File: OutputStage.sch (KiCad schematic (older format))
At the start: 83 parts, among them Q12 BSC067N06LS3, Q13 BSC067N06LS3, Q3 AON7400A, Q5 AON7400A, U5 LM5175PWPR

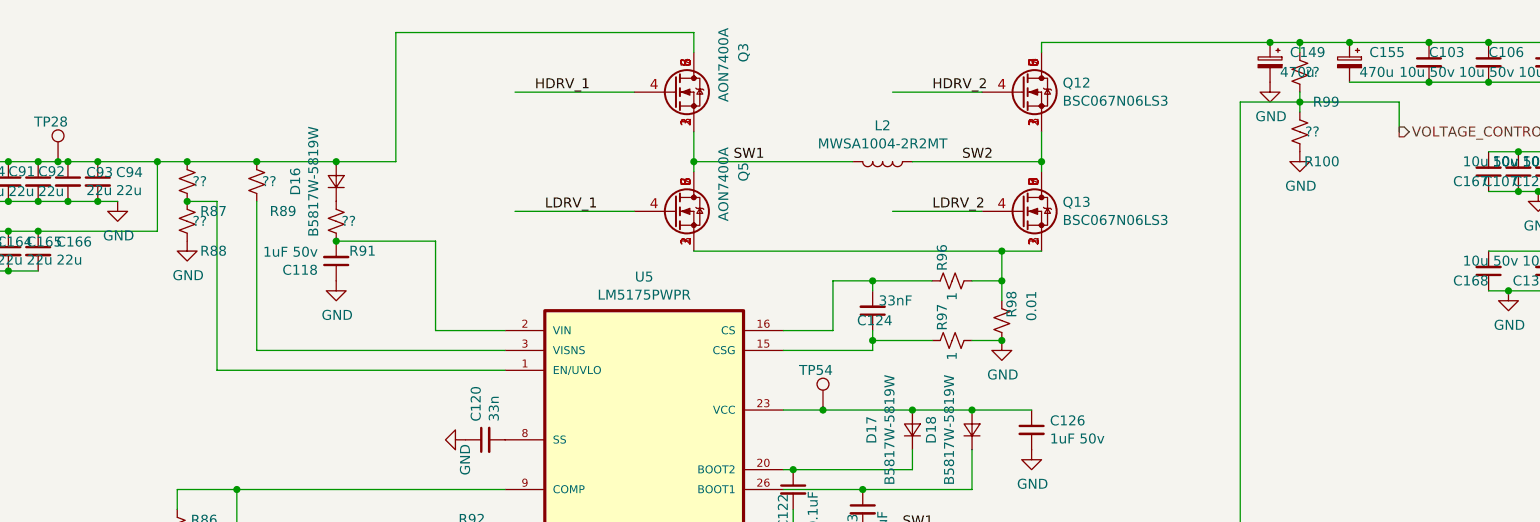
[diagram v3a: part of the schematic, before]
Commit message: Modified connections, added current limit
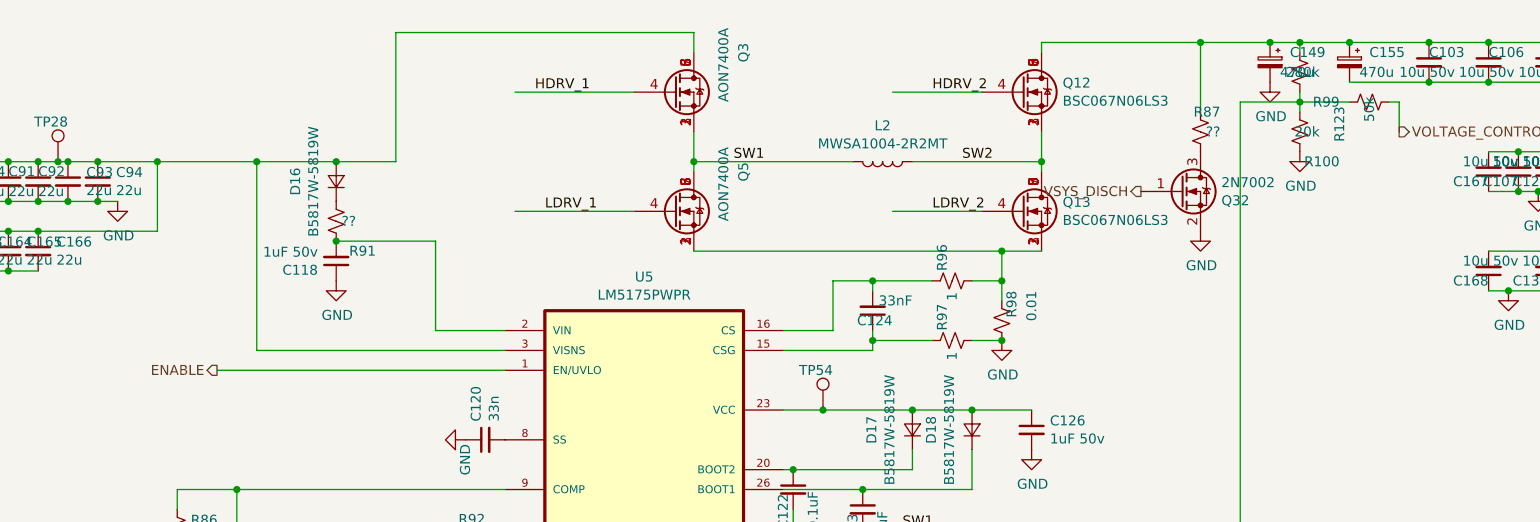
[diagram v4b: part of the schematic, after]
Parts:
- removed R88, R89: ??, lc_lib:0402_R, symbol Device:R_Small_US
- added Q32: 2N7002, Package_TO_SOT_SMD:SOT-23, symbol Device:Q_NMOS_GSD
- added R123: 50k, lc_lib:0402_R, symbol Device:R_Small_US
- R100: value ?? -> 20k
- R99: value ?? -> 280k
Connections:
- net labels added: ENABLE, VSYS_DISCH
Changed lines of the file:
@@
 	2250 1150 2550 1150
 Connection ~ 2250 1150
-$Comp
-L Device:R_Small_US R?
-U 1 1 5FFCD88F
-P 2700 1250
-AR Path="/5FD99B08/5FFCD88F" Ref="R?"  Part="1"
-AR Path="/60413DD6/5FFCD88F" Ref="R87"  Part="1"
-F 0 "R87" H 2500 1400 50  0000 L CNN
-F 1 "??" H 2600 1250 50  0000 L CNN
-F 2 "lc_lib:0402_R" H 2700 1250 50  0001 C CNN
-F 3 "~" H 2700 1250 50  0001 C CNN
-F 4 "C25086" H 2700 1250 50  0001 C CNN "lcsc"
-	1    2700 1250
-	-1   0    0    1
-$EndComp
-Connection ~ 2700 1150
-Wire Wire Line
-	2700 1150 3050 1150
-$Comp
-L Device:R_Small_US R?
-U 1 1 5FFCECFC
-P 2700 1450
-AR Path="/5FD99B08/5FFCECFC" Ref="R?"  Part="1"
-AR Path="/60413DD6/5FFCECFC" Ref="R88"  Part="1"
-F 0 "R88" H 2500 1600 50  0000 L CNN
-F 1 "??" H 2600 1450 50  0000 L CNN
-F 2 "lc_lib:0402_R" H 2700 1450 50  0001 C CNN
-F 3 "~" H 2700 1450 50  0001 C CNN
-F 4 "C25086" H 2700 1450 50  0001 C CNN "lcsc"
-	1    2700 1450
-	-1   0    0    1
-$EndComp
-$Comp
-L power:GND #PWR0202
-U 1 1 5FFCF18A
-P 2700 1550
-F 0 "#PWR0202" H 2700 1300 50  0001 C CNN
-F 1 "GND" H 2705 1377 50  0000 C CNN
-F 2 "" H 2700 1550 50  0001 C CNN
-F 3 "" H 2700 1550 50  0001 C CNN
-	1    2700 1550
-	1    0    0    -1
-$EndComp
 Wire Wire Line
 	4300 2200 2850 2200
-Wire Wire Line
-	2850 2200 2850 1350
-Wire Wire Line
-	2850 1350 2700 1350
-Connection ~ 2700 1350
-$Comp
-L Device:R_Small_US R?
-U 1 1 5FFCFE0F
-P 3050 1250
-AR Path="/5FD99B08/5FFCFE0F" Ref="R?"  Part="1"
-AR Path="/60413DD6/5FFCFE0F" Ref="R89"  Part="1"
-F 0 "R89" H 2850 1400 50  0000 L CNN
-F 1 "??" H 2950 1250 50  0000 L CNN
-F 2 "lc_lib:0402_R" H 3050 1250 50  0001 C CNN
-F 3 "~" H 3050 1250 50  0001 C CNN
-F 4 "C25086" H 3050 1250 50  0001 C CNN "lcsc"
-	1    3050 1250
-	-1   0    0    1
-$EndComp
-Wire Wire Line
-	3050 1350 3050 2100
 Wire Wire Line
 	3050 2100 4300 2100
@@
 Wire Wire Line
 	4950 1400 4350 1400
-Wire Wire Line
-	3050 1150 3450 1150
-Connection ~ 3050 1150
 Connection ~ 3450 1150
 Wire Wire Line
@@
 AR Path="/60413DD6/600521FF" Ref="R99"  Part="1"
 F 0 "R99" H 8100 850 50  0000 L CNN
-F 1 "??" H 8200 700 50  0000 L CNN
+F 1 "280k" H 8200 700 50  0000 L CNN
 F 2 "lc_lib:0402_R" H 8300 700 50  0001 C CNN
 F 3 "~" H 8300 700 50  0001 C CNN
@@
 AR Path="/60413DD6/60053448" Ref="R100"  Part="1"
 F 0 "R100" H 8100 1150 50  0000 L CNN
-F 1 "??" H 8200 1000 50  0000 L CNN
+F 1 "20k" H 8200 1000 50  0000 L CNN
 F 2 "lc_lib:0402_R" H 8300 1000 50  0001 C CNN
 F 3 "~" H 8300 1000 50  0001 C CNN
@@
 	8800 1000 8800 850
 Wire Wire Line
-	8800 850  8300 850
+	8800 850  8750 850
 $Comp
 L SmartBattery:AON7400A Q?
@@
 	2550 1500 1950 1500
 Connection ~ 2550 1150
-Wire Wire Line
-	2550 1150 2700 1150
 Connection ~ 1950 1500
 $Comp
@@
 	1050 1700 900  1700
 Wire Wire Line
-	7000 550  8150 550
+	7000 550  7800 550
 Wire Wire Line
 	5050 5500 4950 5500
@@
 Text HLabel 8800 1000 2    50   Output ~ 0
 VOLTAGE_CONTROL
+Wire Wire Line
+	2550 1150 3050 1150
+Wire Wire Line
+	3050 1150 3050 2100
+Connection ~ 3050 1150
+Wire Wire Line
+	3050 1150 3450 1150
+Text HLabel 2850 2200 0    50   Output ~ 0
+ENABLE
+$Comp
+L Device:Q_NMOS_GSD Q?
+U 1 1 60182DF6
+P 7700 1300
+AR Path="/5FD15753/60182DF6" Ref="Q?"  Part="1"
+AR Path="/600C8F88/60182DF6" Ref="Q?"  Part="1"
+AR Path="/5FF971C1/60182DF6" Ref="Q?"  Part="1"
+AR Path="/60413DD6/60182DF6" Ref="Q32"  Part="1"
+F 0 "Q32" H 7905 1254 50  0000 L CNN
+F 1 "2N7002" H 7905 1345 50  0000 L CNN
+F 2 "Package_TO_SOT_SMD:SOT-23" H 7900 1400 50  0001 C CNN
+F 3 "~" H 7700 1300 50  0001 C CNN
+F 4 "C8545" H 7700 1300 50  0001 C CNN "LCSC"
+	1    7700 1300
+	1    0    0    -1
+$EndComp
+Wire Wire Line
+	7800 900  7800 550
+Connection ~ 7800 550
+Wire Wire Line
+	7800 550  8150 550
+$Comp
+L power:GND #PWR0202
+U 1 1 601B44C1
+P 7800 1500
+F 0 "#PWR0202" H 7800 1250 50  0001 C CNN
+F 1 "GND" H 7805 1327 50  0000 C CNN
+F 2 "" H 7800 1500 50  0001 C CNN
+F 3 "" H 7800 1500 50  0001 C CNN
+	1    7800 1500
+	1    0    0    -1
+$EndComp
+$Comp
+L Device:R_Small_US R?
+U 1 1 601B4BA2
+P 7800 1000
+AR Path="/5FD99B08/601B4BA2" Ref="R?"  Part="1"
+AR Path="/60413DD6/601B4BA2" Ref="R87"  Part="1"
+F 0 "R87" H 7700 900 50  0000 L CNN
+F 1 "??" H 7700 1000 50  0000 L CNN
+F 2 "lc_lib:0402_R" H 7800 1000 50  0001 C CNN
+F 3 "~" H 7800 1000 50  0001 C CNN
+F 4 "C25086" H 7800 1000 50  0001 C CNN "lcsc"
+	1    7800 1000
+	-1   0    0    1
+$EndComp
+Text HLabel 7500 1300 0    50   Output ~ 0
+VSYS_DISCH
+$Comp
+L Device:R_Small_US R?
+U 1 1 60285F33
+P 8650 850
+AR Path="/5FD99B08/60285F33" Ref="R?"  Part="1"
+AR Path="/60413DD6/60285F33" Ref="R123"  Part="1"
+F 0 "R123" H 8450 1000 50  0000 L CNN
+F 1 "50k" H 8550 850 50  0000 L CNN
+F 2 "lc_lib:0402_R" H 8650 850 50  0001 C CNN
+F 3 "~" H 8650 850 50  0001 C CNN
+F 4 "" H 8650 850 50  0001 C CNN "lcsc"
+	1    8650 850
+	0    -1   -1   0
+$EndComp
+Wire Wire Line
+	8550 850  8300 850
 $EndSCHEMATC
